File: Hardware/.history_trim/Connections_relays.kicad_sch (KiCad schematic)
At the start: 10 parts, among them J8 Conn_01x07_Pin

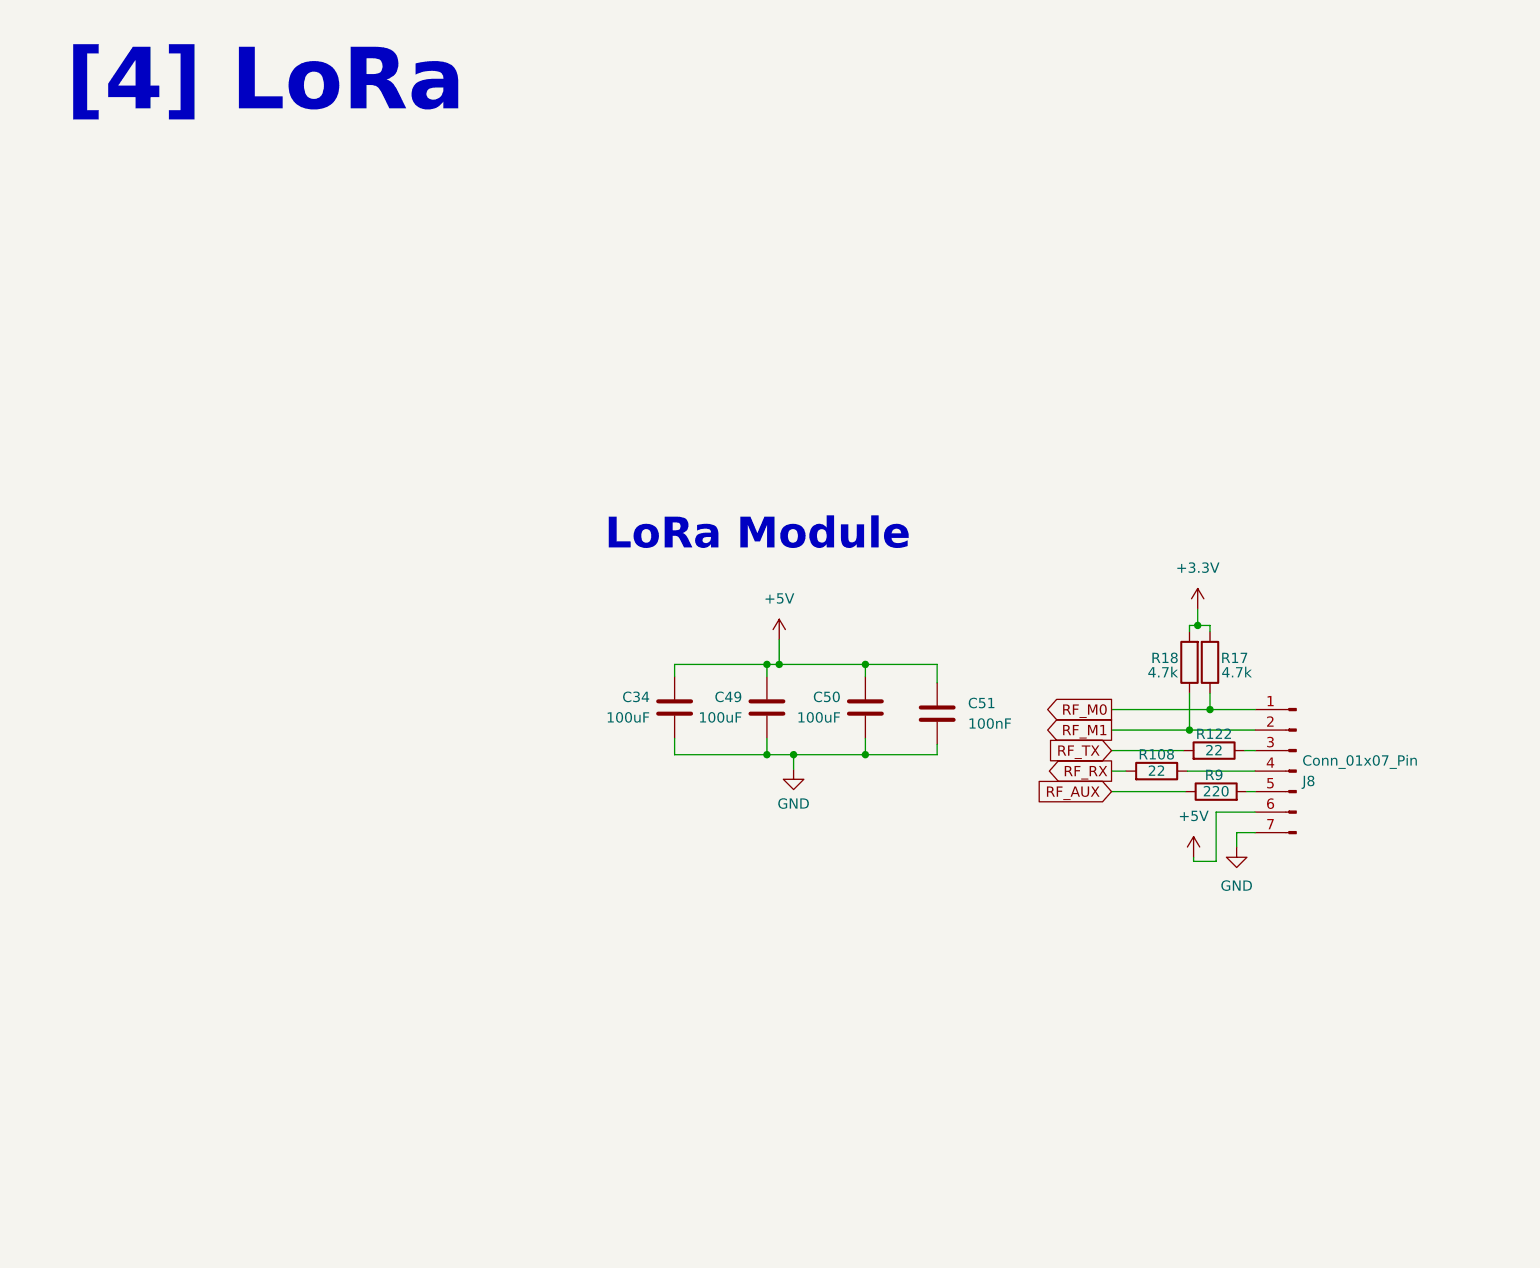
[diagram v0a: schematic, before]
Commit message: Purged heavy binaries and updated gitignore
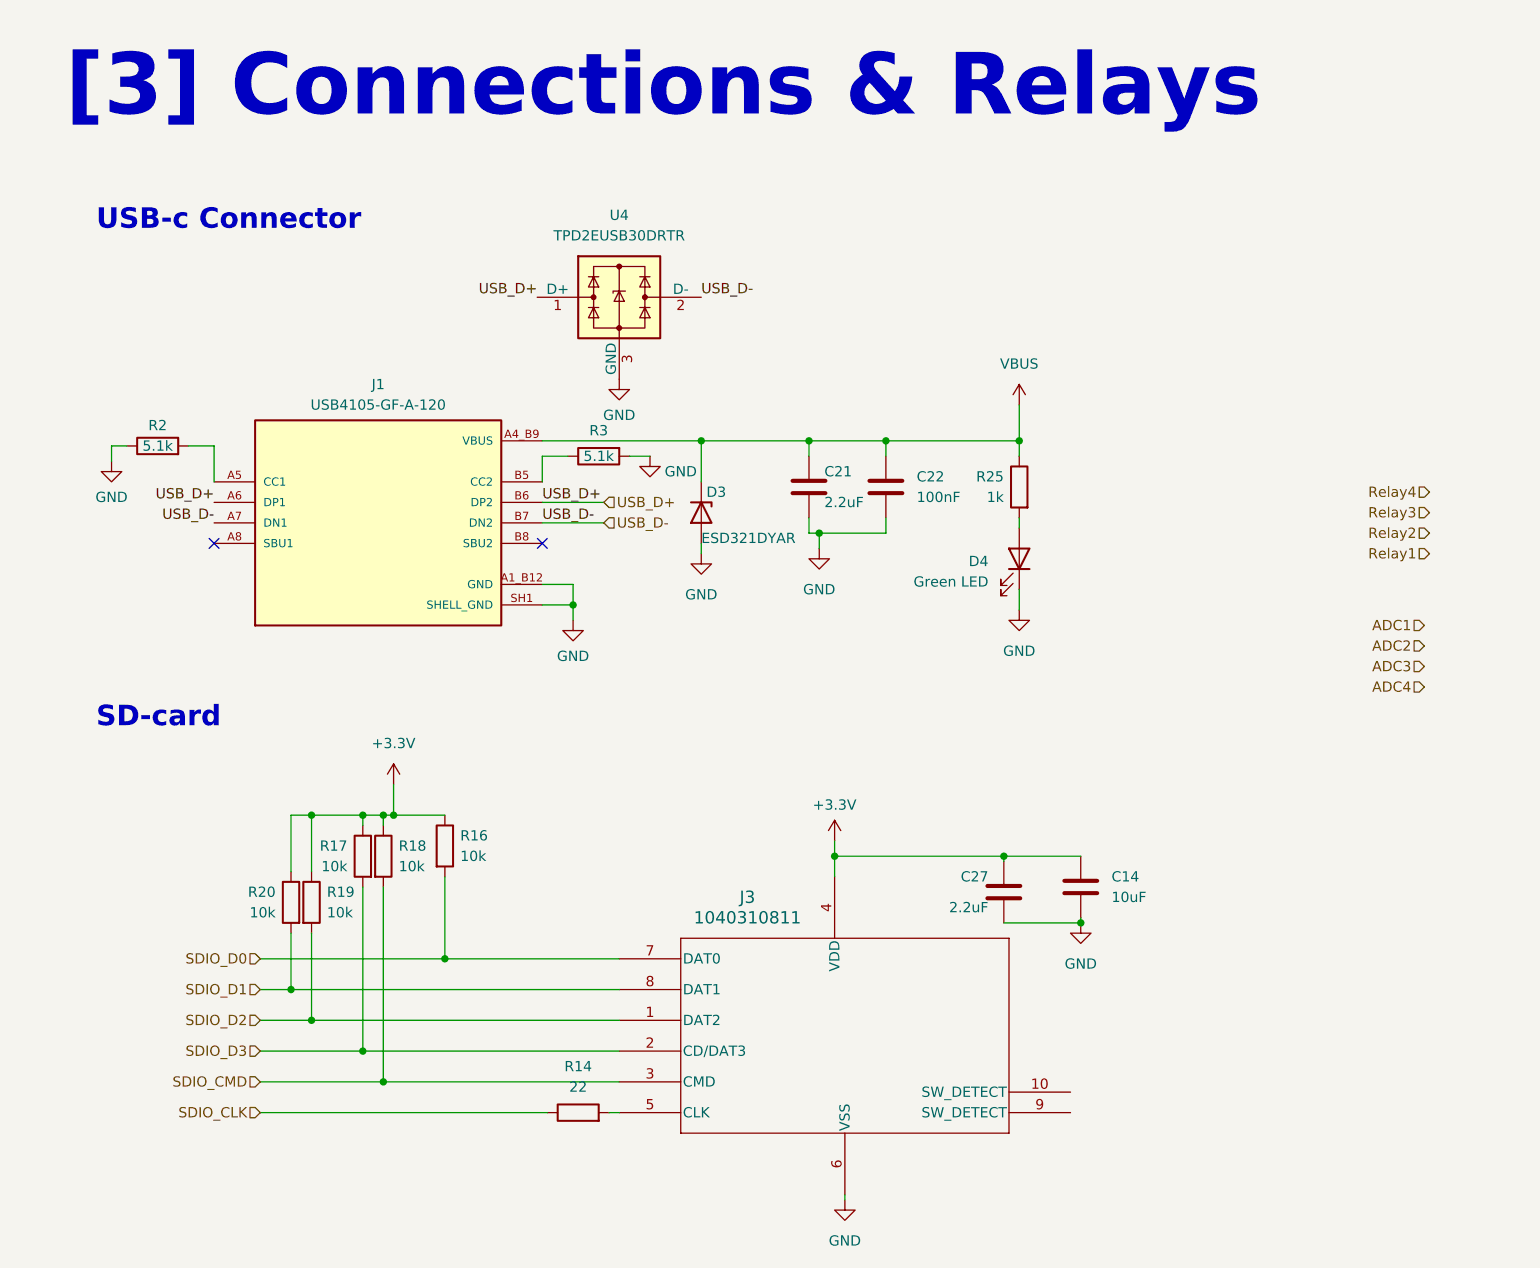
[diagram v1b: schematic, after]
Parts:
- removed C34, C49, C50: 100uF, Capacitor_Tantalum_SMD:CP_EIA-6032-20_AVX-F, symbol Device:C
- removed C51: 100nF, Capacitor_SMD:C_0603_1608Metric, symbol Device:C
- removed J8: Conn_01x07_Pin, footprints:E32-900T30D, symbol Connector:Conn_01x07_Pin
- removed R108, R122: 22, Resistor_SMD:R_0603_1608Metric, symbol Device:R
- removed R9: 220, Resistor_SMD:R_0603_1608Metric, symbol Device:R
- added C14: 10uF, Capacitor_SMD:C_0603_1608Metric, symbol Device:C
- added C21, C27: 2.2uF, Capacitor_SMD:C_0402_1005Metric, symbol Device:C
- added C22: 100nF, Capacitor_SMD:C_0402_1005Metric, symbol Device:C
- added D3: ESD321DYAR, Diode_SMD:D_SOD-523, symbol Diode:ESD5Zxx
- added D4: Green LED, LED_SMD:LED_0603_1608Metric, symbol Device:LED
- added J1: USB4105-GF-A-120, USB4105-GF-A-120:GCT_USB4105-GF-A-120, symbol USB4105-GF-A-120:USB4105-GF-A-120
- added J3: 1040310811, Molex 1040310811:104031-0811_MOL, symbol 2026-07-10_16-12-29:1040310811
- added R14: 22, Resistor_SMD:R_0402_1005Metric, symbol Device:R
- added R16, R19, R20: 10k, Resistor_SMD:R_0603_1608Metric, symbol Device:R
- added R2, R3: 5.1k, Resistor_SMD:R_0402_1005Metric, symbol Device:R
- added R25: 1k, Resistor_SMD:R_0402_1005Metric, symbol Device:R
- added U4: TPD2EUSB30DRTR, Package_TO_SOT_SMD:Texas_DRT-3, symbol Power_Protection:TPD2EUSB30A
- R17, R18: value 4.7k -> 10k; Distributer Link https://www.ozdisan.com/p/smt-smd-ve-cip-direncler-194/roya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 -> https://www.ozdisan.com/p/smt-smd-ve-cip-direncler-194/pana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; Part Number CQ03SAJ0472T5E -> ERJ3EKF1002V
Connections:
- net RF_M0 is gone; now on net +3.3V: R17.1
- net RF_M1 is gone; now on net +3.3V: R18.1
- net +3.3V: now also C14.1, C27.1, J3.4 (VDD), R16.1, R19.1, R20.1; no longer R17.2, R18.2
- net GND: now also C14.2, C21.2, C22.2, C27.2, D3.2 (A), D4.1 (K), J1.A1_B12 (GND), J1.B1_A12 (GND), J1.SH1 (SHELL_GND), J1.SH2 (SHELL_GND), J1.SH3 (SHELL_GND), J1.SH4 (SHELL_GND), J3.6 (VSS), R2.1, R3.2, U4.3 (GND)
- new net: J1.A5 (CC1), R2.2
- new net: J1.B5 (CC2), R3.1
- new net: D4.2 (A), R25.2
- new net: J3.5 (CLK), R14.2
- new net SDIO_CLK: R14.1
- new net SDIO_CMD: J3.3 (CMD), R18.2
- new net SDIO_D0: J3.7 (DAT0), R16.2
- new net SDIO_D1: J3.8 (DAT1), R20.2
- new net SDIO_D2: J3.1 (DAT2), R19.2
- new net SDIO_D3: J3.2 (CD/DAT3), R17.2
- new net USB_D+: J1.A6 (DP1), J1.B6 (DP2), U4.1 (D+)
- new net USB_D-: J1.A7 (DN1), J1.B7 (DN2), U4.2 (D-)
- new net VBUS: C21.1, C22.1, D3.1 (K), J1.A4_B9 (VBUS), J1.B4_A9 (VBUS), R25.1
- no-connect marks 0 -> 2
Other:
- note added: "SD-card"
- note added: "USB-c Connector"
- note added: "[3] Connections & Relays"
- note removed: "LoRa Module"
- note removed: "[4] LoRa"
- title: LoRa -> Connections & Relays
